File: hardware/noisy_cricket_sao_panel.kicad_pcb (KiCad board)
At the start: 2 copper layers, 94 x 52 mm, 226 parts, among them J1 SAO 6-Pin, U1 AD8107, U2 CH32V003F4U6

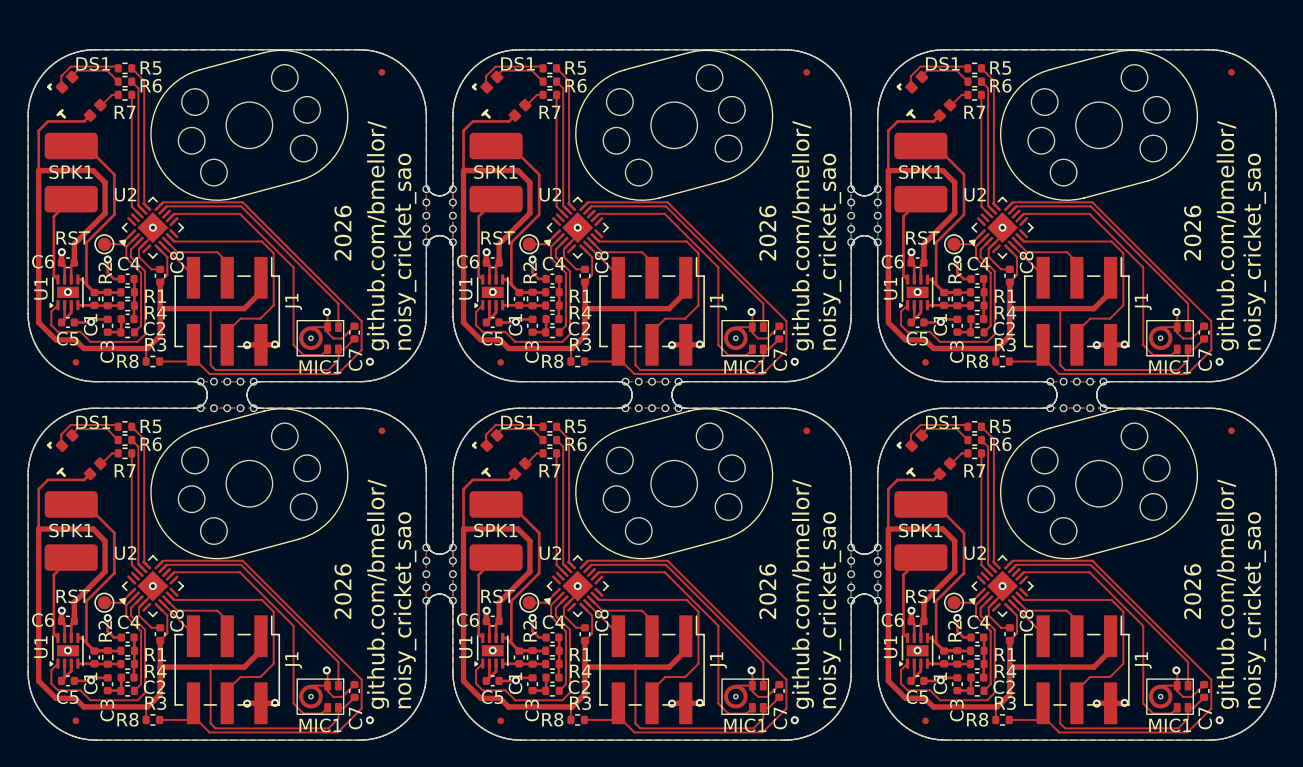
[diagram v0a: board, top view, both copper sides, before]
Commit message: add windowpane to microphone ground ring
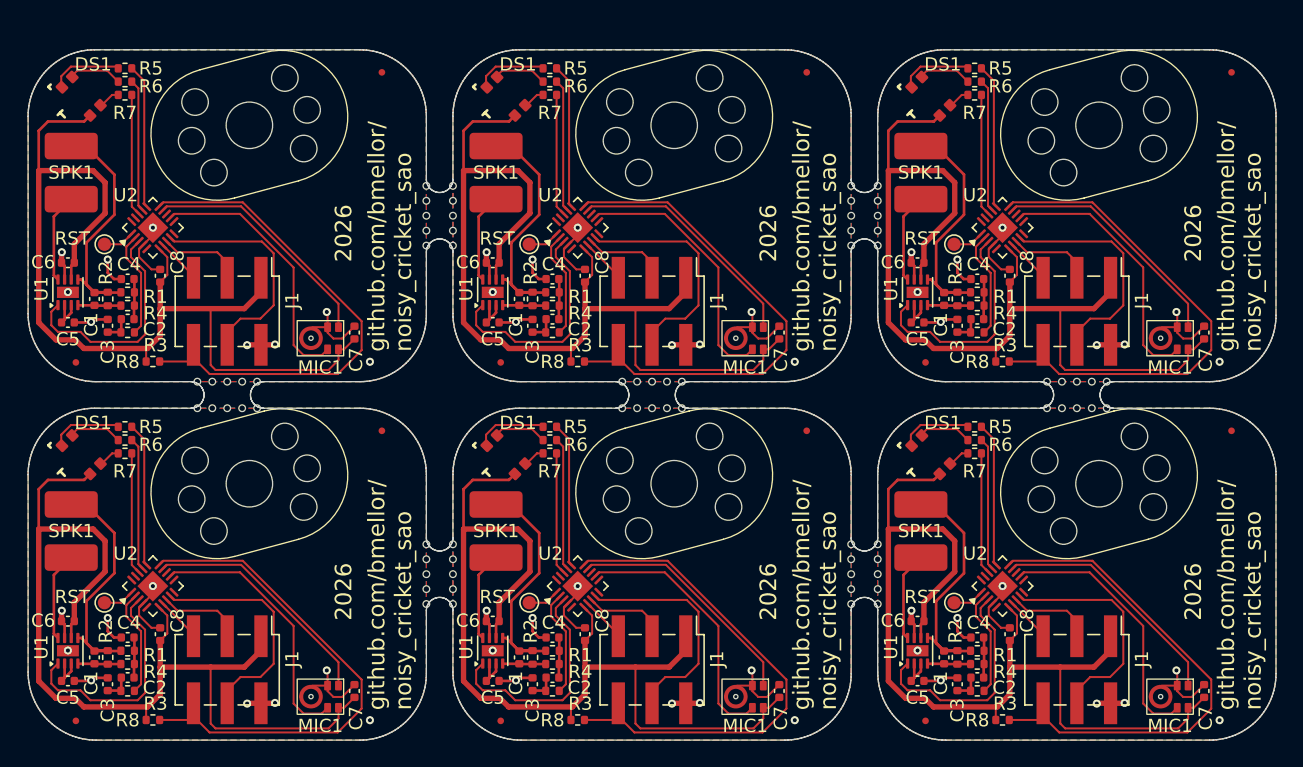
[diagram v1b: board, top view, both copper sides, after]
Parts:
- moved KiKit_MB_10_1 0.25 mm to (133.5, 61.8)
- moved KiKit_MB_10_5 0.25 mm to (133.5, 57.2)
- moved KiKit_MB_11_1 0.25 mm to (163.5, 57.2)
- moved KiKit_MB_11_5 0.25 mm to (163.5, 61.8)
- moved KiKit_MB_12_1 0.25 mm to (146.2, 47.0)
- moved KiKit_MB_12_5 0.25 mm to (150.8, 47.0)
- moved KiKit_MB_13_1 0.25 mm to (165.5, 61.8)
- moved KiKit_MB_13_5 0.25 mm to (165.5, 57.2)
- moved KiKit_MB_14_1 0.25 mm to (178.2, 47.0)
- moved KiKit_MB_14_5 0.25 mm to (182.8, 47.0)
- moved KiKit_MB_1_1 0.25 mm to (131.5, 30.2)
- moved KiKit_MB_1_5 0.25 mm to (131.5, 34.8)
- moved KiKit_MB_2_1 0.25 mm to (118.8, 45.0)
- moved KiKit_MB_2_5 0.25 mm to (114.2, 45.0)
- moved KiKit_MB_3_1 0.25 mm to (133.5, 34.8)
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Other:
- outline, holes or cut-outs redrawn
